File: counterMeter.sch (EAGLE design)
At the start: 129 parts, among them IC1 74AC14D, IC2 REG1117, IC3 74AC74D, IC4 74HC151D, IC5 74AC390D, IC6 74HC595D, IC7 74HC595D, J1 COMMON, J2 U/I/R, J3 10A, K1 G6K-2P-Y, K2 G6K-2P-Y, K3 G6K-2P-Y, K4 G6K-2P-Y, K5 G6K-2P-Y, T1 BC847, T10 BC847, T2 BC847, T3 BC847, T4 BC847, T5 BC857, T6 BC857, T7 BC857, T8 BC857, T9 BC857, U1 MAX9201, U2 74XX161, U3 SN74LVC2G157DCTR, U4 MAX871, U5 AD8638, U6 AD8539

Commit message: some pin changes in schematic + first draw of the PCB layout
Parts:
- removed IN_LF1: 1-227161-6, con-coax:1-227161-6
- removed R14, R15: 330, resistor:R-EU_R0603
- added D11: 4148, diode:DIODE-SOD323-W
- added J4: U/I/R, dmm:4MMJACK
- R12, R13: value 330 -> 10k
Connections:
- removed net N$19: IC4A.D0, U2G$1.QA
- removed net N$20: R13.1, U1D.IN-
- removed net N$21: R15.1, U1B.IN-
- removed net N$22: R14.1, U1B.IN+
- removed net N$23: R12.1, U1D.IN+
- removed net SIGN: R23.2, T1.C
- new net CNT_IN_: IC4A.D4, R13.2
- new net LF_SIG: IC3A.CLK, R12.2, U1A.OUT
- new net N$14: IC4A.D3, U2G$1.QA
- new net U_I_R_RAW: K52.P, U5G1.IN+
- net CNT_IN: now also R13.1; no longer IC4A.D4
- net DIVSEL1: now also IC6A.QC; no longer IC6A.QB
- net DIVSEL2: now also IC6A.QD; no longer IC6A.QC
- net DIVSEL3: now also IC6A.QE; no longer IC6A.QD
- net GND: now also U1B.IN+, U1B.IN-, U1D.IN+, U1D.IN-; no longer IN_LF1.2, R13.2, R15.2
- net HFSEL1: now also IC6A.QG; no longer IC6A.QF
- net HFSEL2: now also IC6A.QF; no longer IC6A.QG
- net INPUTSEL: now also IC6A.QB; no longer IC6A.QE
- net I_U/I/R: now also K53.P; no longer K52.P
- net LF_DIRECT: now also R12.1; no longer IC3A.CLK, U1A.OUT
- net N$16: now also IC4A.D2, U2G$1.QB; no longer IC4A.D3, U2G$1.QD
- net N$17: now also IC4A.D1; no longer IC4A.D2
- net N$18: now also IC4A.D0, U2G$1.QD; no longer IC4A.D1, U2G$1.QB
- net N$45: now also D11.A
- net N$51: now also K53.O; no longer K52.O
- net N$9: now also J4.1; no longer IN_LF1.1
- net PB2: now also R23.2, T1.C; no longer DMM_LEFT.6
- net RANGE_LSB: now also IC6A.QH; no longer IC7A.QF
- net RANGE_MSB: now also IC7A.QA; no longer IC7A.QE
- net R_RANGE1: now also IC7A.QF; no longer IC7A.QD
- net R_RANGE2: now also IC7A.QE; no longer IC7A.QC
- net R_RANGE3: now also IC7A.QD; no longer IC7A.QB
- net R_RANGE4: now also IC7A.QC; no longer IC7A.QA
- net R_RANGE5: now also IC7A.QB; no longer IC6A.QH
- net U_I_RAW: now also K52.O; no longer K53.O, K53.P, U5G1.IN+
- net VCC: now also D11.C; no longer R12.2, R14.2
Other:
- moved on the sheet: C5, D1, D2, IC1A, K5, R10, R11, R12, R13, R9

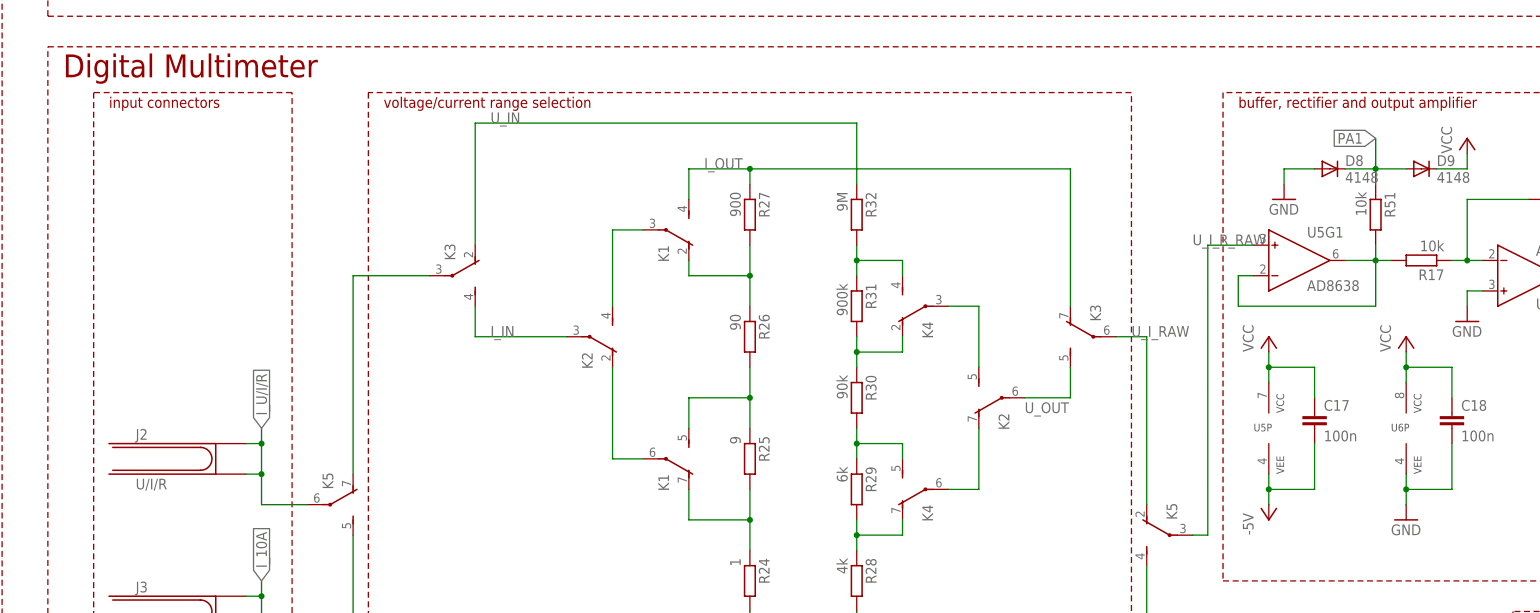
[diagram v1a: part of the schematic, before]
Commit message: some input protection + buffer output filter
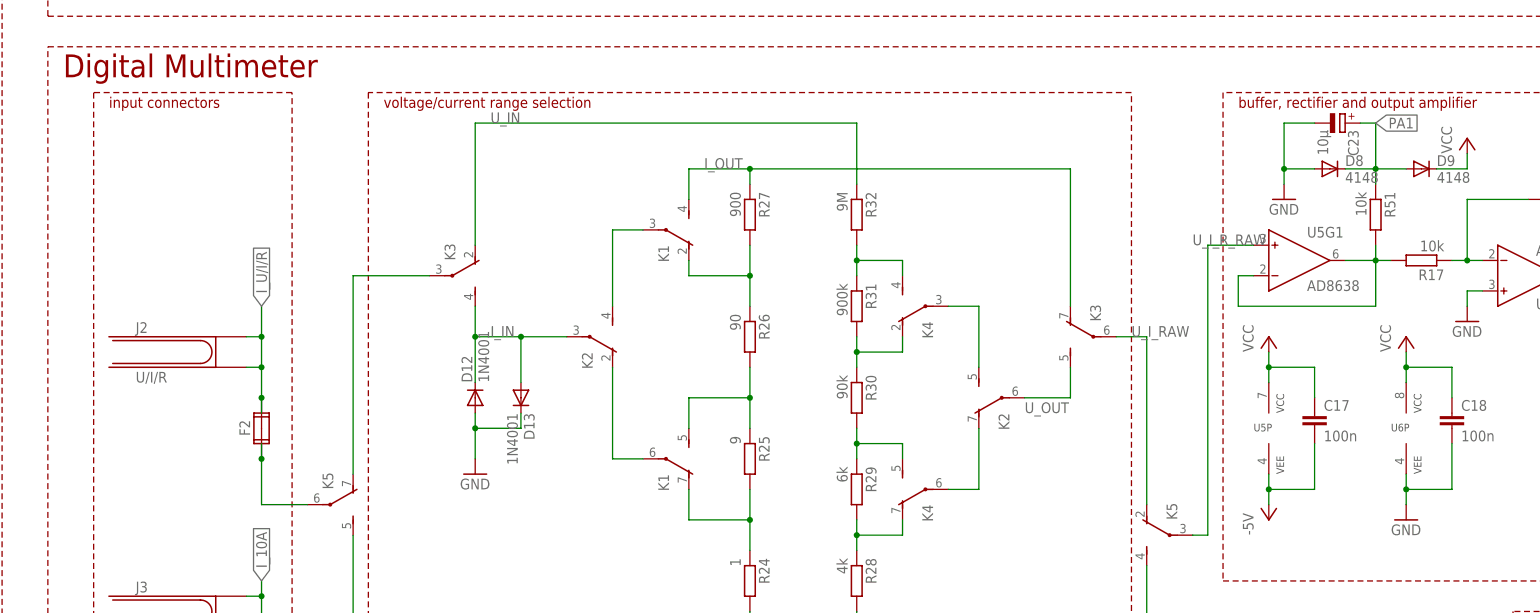
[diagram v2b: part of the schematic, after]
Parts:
- added C23: 10µ, rcl:CPOL-EUE2-5
- added D12, D13: 1N4001, diode:1N4004
- added F2: (no value), special:FUSE2P
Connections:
- new net N$19: F2.1A, F2.1B, K53.P
- net GND: now also C23.-, D12.A, D13.C
- net I_IN: now also D12.C, D13.A
- net I_U/I/R: now also F2.2A, F2.2B; no longer K53.P
- net PA1: now also C23.+
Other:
- moved on the sheet: J2
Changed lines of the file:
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@@
 <part name="R12" library="resistor" deviceset="R-EU_" device="R0603" value="10k"/>
 <part name="R13" library="resistor" deviceset="R-EU_" device="R0603" value="10k"/>
+<part name="D12" library="diode" deviceset="1N4004" device="" value="1N4001"/>
+<part name="D13" library="diode" deviceset="1N4004" device="" value="1N4001"/>
+<part name="GND7" library="supply1" deviceset="GND" device=""/>
+<part name="F2" library="special" deviceset="FUSE2P" device=""/>
+<part name="C23" library="rcl" deviceset="CPOL-EU" device="E2-5" value="10µ"/>
 </parts>
 <sheets>
@@
 <instance part="K2" gate="3" x="469.9" y="106.68" rot="MR270"/>
 <instance part="J1" gate="G$1" x="337.82" y="48.26"/>
-<instance part="J2" gate="G$1" x="337.82" y="96.52"/>
+<instance part="J2" gate="G$1" x="337.82" y="114.3"/>
 <instance part="J3" gate="G$1" x="337.82" y="71.12"/>
 <instance part="GND19" gate="1" x="345.44" y="40.64"/>
@@
 <instance part="R12" gate="G$1" x="60.96" y="-40.64" rot="R180"/>
 <instance part="R13" gate="G$1" x="177.8" y="73.66" rot="R270"/>
+<instance part="D12" gate="1" x="381" y="106.68" rot="R90"/>
+<instance part="D13" gate="1" x="388.62" y="106.68" rot="R270"/>
+<instance part="GND7" gate="1" x="381" y="93.98"/>
+<instance part="F2" gate="G$1" x="345.44" y="101.6" rot="R90"/>
+<instance part="C23" gate="G$1" x="525.78" y="152.4" rot="R270"/>
 </instances>
 <busses>
@@
 <wire x1="520.7" y1="144.78" x2="515.62" y2="144.78" width="0.1524" layer="91"/>
 <wire x1="515.62" y1="144.78" x2="515.62" y2="142.24" width="0.1524" layer="91"/>
+<pinref part="C23" gate="G$1" pin="-"/>
+<wire x1="520.7" y1="152.4" x2="515.62" y2="152.4" width="0.1524" layer="91"/>
+<wire x1="515.62" y1="152.4" x2="515.62" y2="144.78" width="0.1524" layer="91"/>
+<junction x="515.62" y="144.78"/>
 </segment>
 <segment>
@@
 <wire x1="350.52" y1="193.04" x2="345.44" y2="193.04" width="0.1524" layer="91"/>
 <wire x1="345.44" y1="193.04" x2="345.44" y2="185.42" width="0.1524" layer="91"/>
+</segment>
+<segment>
+<pinref part="D12" gate="1" pin="A"/>
+<pinref part="GND7" gate="1" pin="GND"/>
+<wire x1="381" y1="104.14" x2="381" y2="101.6" width="0.1524" layer="91"/>
+<pinref part="D13" gate="1" pin="C"/>
+<wire x1="381" y1="101.6" x2="381" y2="96.52" width="0.1524" layer="91"/>
+<wire x1="381" y1="101.6" x2="388.62" y2="101.6" width="0.1524" layer="91"/>
+<wire x1="388.62" y1="101.6" x2="388.62" y2="104.14" width="0.1524" layer="91"/>
+<junction x="381" y="101.6"/>
 </segment>
 </net>
@@
 <pinref part="J2" gate="G$1" pin="2"/>
 <pinref part="J2" gate="G$1" pin="1"/>
-<wire x1="345.44" y1="93.98" x2="342.9" y2="93.98" width="0.1524" layer="91"/>
-<wire x1="342.9" y1="99.06" x2="345.44" y2="99.06" width="0.1524" layer="91"/>
-<wire x1="345.44" y1="99.06" x2="345.44" y2="93.98" width="0.1524" layer="91"/>
-<wire x1="345.44" y1="99.06" x2="345.44" y2="101.6" width="0.1524" layer="91"/>
-<junction x="345.44" y="99.06"/>
-<label x="345.44" y="101.6" size="1.778" layer="95" rot="R90" xref="yes"/>
-<pinref part="K5" gate="3" pin="P"/>
-<wire x1="353.06" y1="88.9" x2="345.44" y2="88.9" width="0.1524" layer="91"/>
-<wire x1="345.44" y1="88.9" x2="345.44" y2="93.98" width="0.1524" layer="91"/>
-<junction x="345.44" y="93.98"/>
+<wire x1="345.44" y1="111.76" x2="342.9" y2="111.76" width="0.1524" layer="91"/>
+<wire x1="342.9" y1="116.84" x2="345.44" y2="116.84" width="0.1524" layer="91"/>
+<wire x1="345.44" y1="116.84" x2="345.44" y2="111.76" width="0.1524" layer="91"/>
+<wire x1="345.44" y1="116.84" x2="345.44" y2="121.92" width="0.1524" layer="91"/>
+<junction x="345.44" y="116.84"/>
+<label x="345.44" y="121.92" size="1.778" layer="95" rot="R90" xref="yes"/>
+<junction x="345.44" y="111.76"/>
+<pinref part="F2" gate="G$1" pin="2A"/>
+<wire x1="345.44" y1="104.14" x2="345.44" y2="106.68" width="0.1524" layer="91"/>
+<wire x1="345.44" y1="106.68" x2="345.44" y2="111.76" width="0.1524" layer="91"/>
+<junction x="345.44" y="106.68"/>
+<pinref part="F2" gate="G$1" pin="2B"/>
 </segment>
 </net>
@@
 <segment>
 <pinref part="K2" gate="2" pin="P"/>
-<wire x1="396.24" y1="116.84" x2="381" y2="116.84" width="0.1524" layer="91"/>
+<wire x1="396.24" y1="116.84" x2="388.62" y2="116.84" width="0.1524" layer="91"/>
 <label x="383.54" y="116.84" size="1.778" layer="95"/>
 <pinref part="K3" gate="2" pin="S"/>
+<wire x1="388.62" y1="116.84" x2="381" y2="116.84" width="0.1524" layer="91"/>
 <wire x1="381" y1="116.84" x2="381" y2="121.92" width="0.1524" layer="91"/>
+<wire x1="381" y1="109.22" x2="381" y2="116.84" width="0.1524" layer="91"/>
+<junction x="381" y="116.84"/>
+<pinref part="D12" gate="1" pin="C"/>
+<pinref part="D13" gate="1" pin="A"/>
+<wire x1="388.62" y1="109.22" x2="388.62" y2="116.84" width="0.1524" layer="91"/>
+<junction x="388.62" y="116.84"/>
 </segment>
 </net>
@@
 <wire x1="530.86" y1="142.24" x2="530.86" y2="144.78" width="0.1524" layer="91"/>
 <junction x="530.86" y="144.78"/>
-<label x="530.86" y="149.86" size="1.778" layer="95" rot="R180" xref="yes"/>
-<wire x1="530.86" y1="144.78" x2="530.86" y2="149.86" width="0.1524" layer="91"/>
+<label x="530.86" y="152.4" size="1.778" layer="95" xref="yes"/>
+<wire x1="530.86" y1="144.78" x2="530.86" y2="152.4" width="0.1524" layer="91"/>
+<pinref part="C23" gate="G$1" pin="+"/>
+<wire x1="528.32" y1="152.4" x2="530.86" y2="152.4" width="0.1524" layer="91"/>
 </segment>
 </net>
@@
 </segment>
 </net>
+<net name="N$19" class="0">
+<segment>
+<pinref part="F2" gate="G$1" pin="1B"/>
+<pinref part="F2" gate="G$1" pin="1A"/>
+<wire x1="345.44" y1="96.52" x2="345.44" y2="99.06" width="0.1524" layer="91"/>
+<junction x="345.44" y="96.52"/>
+<pinref part="K5" gate="3" pin="P"/>
+<wire x1="353.06" y1="88.9" x2="345.44" y2="88.9" width="0.1524" layer="91"/>
+<wire x1="345.44" y1="88.9" x2="345.44" y2="96.52" width="0.1524" layer="91"/>
+</segment>
+</net>

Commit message: more minor pcb changes
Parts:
- F2: value (none) -> 315mA
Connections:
- net N$9: now also J4.2
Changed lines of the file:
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@@
 <part name="D13" library="diode" deviceset="1N4004" device="" value="1N4001"/>
 <part name="GND7" library="supply1" deviceset="GND" device=""/>
-<part name="F2" library="special" deviceset="FUSE2P" device=""/>
+<part name="F2" library="special" deviceset="FUSE2P" device="" value="315mA"/>
 <part name="C23" library="rcl" deviceset="CPOL-EU" device="E2-5" value="10µ"/>
 </parts>
@@
 <pinref part="J4" gate="G$1" pin="1"/>
 <wire x1="-12.7" y1="83.82" x2="-10.16" y2="83.82" width="0.1524" layer="91"/>
+<pinref part="J4" gate="G$1" pin="2"/>
+<wire x1="-12.7" y1="78.74" x2="-10.16" y2="78.74" width="0.1524" layer="91"/>
+<wire x1="-10.16" y1="78.74" x2="-10.16" y2="83.82" width="0.1524" layer="91"/>
+<junction x="-10.16" y="83.82"/>
 </segment>
 </net>
